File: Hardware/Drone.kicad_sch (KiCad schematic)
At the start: 6 parts

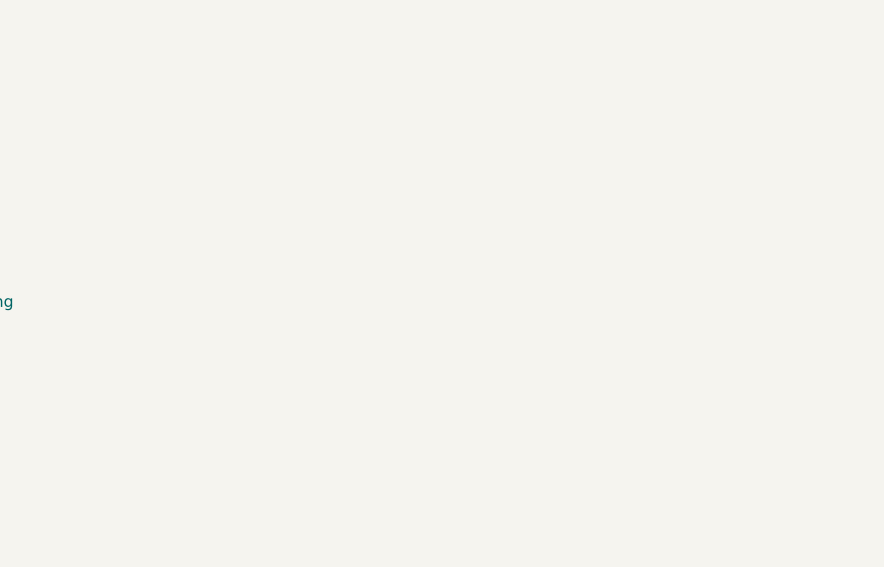
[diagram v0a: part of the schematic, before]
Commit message: boosted pid controller
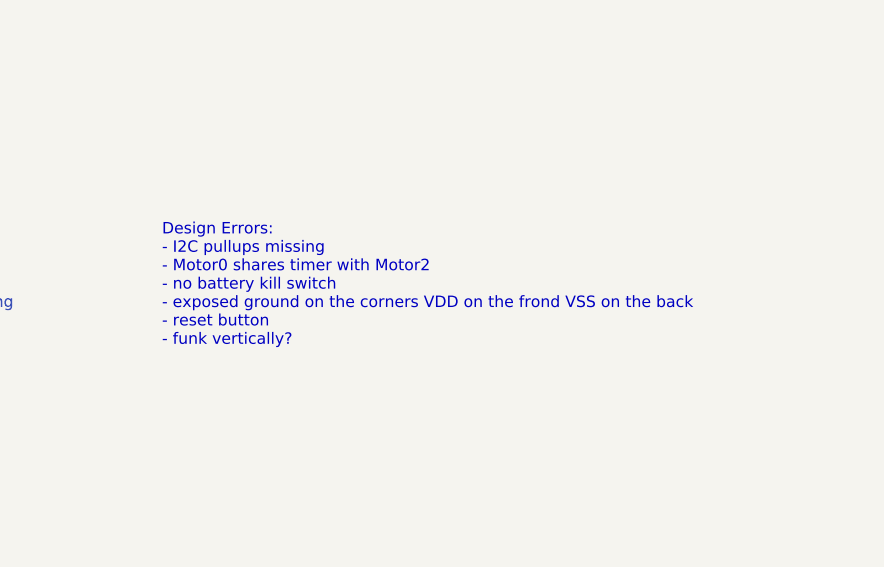
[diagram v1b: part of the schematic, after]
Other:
- note added: "Design Errors: - I2C pullups missing - Motor0 shares timer with Motor2 - no battery kill switch - exposed ground on the corners VDD on the frond VSS on the back - reset button - funk vertically?"
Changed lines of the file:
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@@
+		)
+	)
+	(text "Design Errors:\n- I2C pullups missing\n- Motor0 shares timer with Motor2\n- no battery kill switch\n- exposed ground on the corners VDD on the frond VSS on the back\n- reset button\n- funk vertically?"
+		(exclude_from_sim no)
+		(at 196.342 90.424 0)
+		(effects
+			(font
+				(size 1.27 1.27)
+			)
+			(justify left)
 		)
 	)
